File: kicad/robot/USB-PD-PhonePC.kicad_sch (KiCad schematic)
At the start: 44 parts, among them IC1 TPS61253AYFFR, U11 MAX77958EWV+T, U15 ESD122DMYR

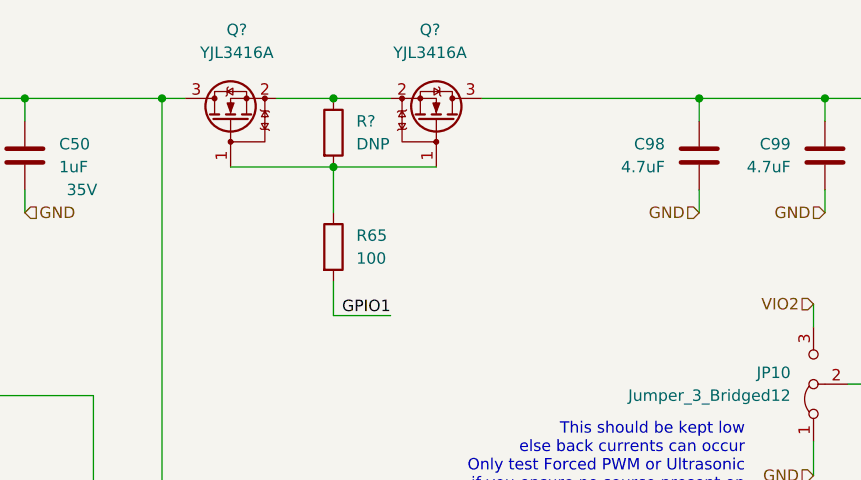
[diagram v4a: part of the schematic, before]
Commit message: Updating mosfets to load switch on phone side USB
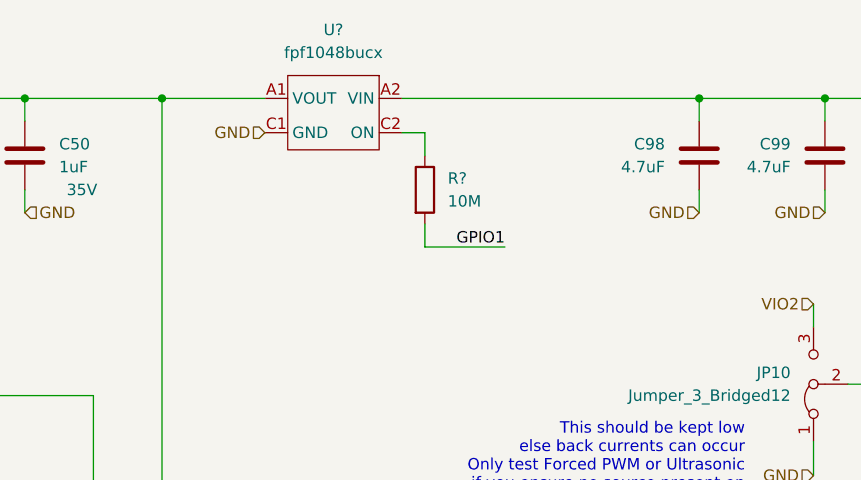
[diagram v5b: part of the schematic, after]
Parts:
- removed Q? (x2): YJL3416A, Package_TO_SOT_SMD:SOT-23, symbol Transistor_FET:YJL3416A
- removed R65: 100, Resistor_SMD:R_0603_1608Metric, symbol Device:R
- removed R?: DNP, Resistor_SMD:R_0603_1608Metric, symbol Device:R
- added R?: 10M, Resistor_SMD:R_0603_1608Metric, symbol Device:R
- added U?: fpf1048bucx, Package_BGA:BGA6N50P3X2_146X96X62N, symbol Power_Management:fpf1048bucx
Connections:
- net GND: now also U?.C1 (GND)
- net GPIO1: now also R?.2
- net at C100.1, C98.1, C99.1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: now also U?.A2 (VIN), U?.B2 (VIN)
- net at C50.1, JP4.2 (B), U11.A6 (VBUS): now also U?.A1 (VOUT), U?.B1 (VOUT)
- new net: R?.1, U?.C2 (ON)
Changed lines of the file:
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@@
   (junction (at 287.02 293.37) (diameter 0) (color 0 0 0 0)
   )
-  (junction (at 267.97 128.27) (diameter 0) (color 0 0 0 0)
-  )
   (junction (at 322.58 120.65) (diameter 0) (color 0 0 0 0)
   )
@@
   )
   (junction (at 236.22 267.97) (diameter 0) (color 0 0 0 0)
-  )
-  (junction (at 267.97 120.65) (diameter 0) (color 0 0 0 0)
   )
   (junction (at 187.96 201.93) (diameter 0) (color 0 0 0 0)
@@
     (stroke (width 0) (type default) (color 0 0 0 0))
   )
-  (wire (pts (xy 267.97 140.97) (xy 267.97 144.78))
-    (stroke (width 0) (type default) (color 0 0 0 0))
-  )
   (wire (pts (xy 397.51 120.65) (xy 410.21 120.65))
     (stroke (width 0) (type default) (color 0 0 0 0))
@@
     (stroke (width 0) (type default) (color 0 0 0 0))
   )
+  (wire (pts (xy 275.59 124.46) (xy 278.13 124.46))
+    (stroke (width 0) (type default) (color 0 0 0 0))
+  )
   (wire (pts (xy 213.36 175.26) (xy 213.36 180.34))
     (stroke (width 0) (type default) (color 0 0 0 0))
@@
     (stroke (width 0) (type default) (color 0 0 0 0))
   )
+  (wire (pts (xy 278.13 134.62) (xy 278.13 137.16))
+    (stroke (width 0) (type default) (color 0 0 0 0))
+  )
   (wire (pts (xy 353.06 280.67) (xy 353.06 283.21))
     (stroke (width 0) (type default) (color 0 0 0 0))
@@
     (stroke (width 0) (type default) (color 0 0 0 0))
   )
+  (wire (pts (xy 248.92 120.65) (xy 260.35 120.65))
+    (stroke (width 0) (type default) (color 0 0 0 0))
+  )
   (wire (pts (xy 331.47 152.4) (xy 331.47 140.97))
     (stroke (width 0) (type default) (color 0 0 0 0))
@@
     (stroke (width 0) (type default) (color 0 0 0 0))
   )
-  (wire (pts (xy 267.97 144.78) (xy 274.32 144.78))
+  (wire (pts (xy 278.13 137.16) (xy 287.02 137.16))
     (stroke (width 0) (type default) (color 0 0 0 0))
   )
@@
     (stroke (width 0) (type default) (color 0 0 0 0))
   )
-  (wire (pts (xy 261.62 120.65) (xy 267.97 120.65))
-    (stroke (width 0) (type default) (color 0 0 0 0))
-  )
   (wire (pts (xy 309.88 254) (xy 316.23 254))
     (stroke (width 0) (type default) (color 0 0 0 0))
@@
     (stroke (width 0) (type default) (color 0 0 0 0))
   )
+  (wire (pts (xy 278.13 124.46) (xy 278.13 127))
+    (stroke (width 0) (type default) (color 0 0 0 0))
+  )
   (wire (pts (xy 219.71 262.89) (xy 219.71 267.97))
     (stroke (width 0) (type default) (color 0 0 0 0))
@@
     (stroke (width 0) (type default) (color 0 0 0 0))
   )
-  (wire (pts (xy 267.97 128.27) (xy 267.97 133.35))
-    (stroke (width 0) (type default) (color 0 0 0 0))
-  )
   (wire (pts (xy 309.88 259.08) (xy 316.23 259.08))
     (stroke (width 0) (type default) (color 0 0 0 0))
@@
     (stroke (width 0) (type default) (color 0 0 0 0))
   )
-  (wire (pts (xy 256.54 128.27) (xy 267.97 128.27))
-    (stroke (width 0) (type default) (color 0 0 0 0))
-  )
   (wire (pts (xy 379.73 120.65) (xy 375.92 120.65))
     (stroke (width 0) (type default) (color 0 0 0 0))
@@
     (stroke (width 0) (type default) (color 0 0 0 0))
   )
-  (wire (pts (xy 267.97 128.27) (xy 279.4 128.27))
-    (stroke (width 0) (type default) (color 0 0 0 0))
-  )
   (wire (pts (xy 200.66 120.65) (xy 213.36 120.65))
     (stroke (width 0) (type default) (color 0 0 0 0))
@@
     (stroke (width 0) (type default) (color 0 0 0 0))
   )
-  (wire (pts (xy 248.92 120.65) (xy 251.46 120.65))
-    (stroke (width 0) (type default) (color 0 0 0 0))
-  )
   (wire (pts (xy 336.55 120.65) (xy 342.9 120.65))
     (stroke (width 0) (type default) (color 0 0 0 0))
@@
     (stroke (width 0) (type default) (color 0 0 0 0))
   )
-  (wire (pts (xy 267.97 120.65) (xy 274.32 120.65))
-    (stroke (width 0) (type default) (color 0 0 0 0))
-  )
   (wire (pts (xy 175.26 228.6) (xy 193.04 228.6))
     (stroke (width 0) (type default) (color 0 0 0 0))
@@
     (stroke (width 0) (type default) (color 0 0 0 0))
   )
-  (wire (pts (xy 284.48 120.65) (xy 308.61 120.65))
+  (wire (pts (xy 275.59 120.65) (xy 308.61 120.65))
     (stroke (width 0) (type default) (color 0 0 0 0))
   )
@@
     (effects (font (size 1.27 1.27)) (justify right bottom))
   )
-  (label "GPIO1" (at 274.32 144.78 180)
+  (label "GPIO1" (at 287.02 137.16 180)
     (effects (font (size 1.27 1.27)) (justify right bottom))
   )
@@
   )
   (hierarchical_label "GND" (shape input) (at 321.31 162.56 180)
+    (effects (font (size 1.27 1.27)) (justify right))
+  )
+  (hierarchical_label "GND" (shape input) (at 260.35 124.46 180)
     (effects (font (size 1.27 1.27)) (justify right))
   )
@@
     (pin "2")
   )
-  (symbol (lib_id "Transistor_FET:YJL3416A") (at 279.4 123.19 270) (mirror x) (unit 1)
-    (in_bom yes) (on_board yes) (fields_autoplaced)
-    (property "Reference" "Q?" (id 0) (at 278.7015 113.03 90))
-    (property "Value" "YJL3416A" (id 1) (at 278.7015 115.57 90))
-    (property "Footprint" "Package_TO_SOT_SMD:SOT-23" (id 2) (at 277.495 118.11 0)
-      (effects (font (size 1.27 1.27)) (justify left) hide)
-    )
-    (property "Datasheet" "https://www.21yangjie.com/style/pdf/low-voltage-mosfet/YJL3416A.pdf" (id 3) (at 279.4 123.19 0)
-      (effects (font (size 1.27 1.27)) hide)
-    )
-    (pin "1")
-    (pin "2")
-    (pin "3")
-  )
   (symbol (lib_id "Jumper:Jumper_2_Bridged") (at 177.8 201.93 0) (unit 1)
     (in_bom yes) (on_board yes) (fields_autoplaced)
@@
     (pin "1")
   )
-  (symbol (lib_id "Transistor_FET:YJL3416A") (at 256.54 123.19 90) (unit 1)
-    (in_bom yes) (on_board yes) (fields_autoplaced)
-    (property "Reference" "Q?" (id 0) (at 257.2385 113.03 90))
-    (property "Value" "YJL3416A" (id 1) (at 257.2385 115.57 90))
-    (property "Footprint" "Package_TO_SOT_SMD:SOT-23" (id 2) (at 258.445 118.11 0)
-      (effects (font (size 1.27 1.27)) (justify left) hide)
-    )
-    (property "Datasheet" "https://www.21yangjie.com/style/pdf/low-voltage-mosfet/YJL3416A.pdf" (id 3) (at 256.54 123.19 0)
-      (effects (font (size 1.27 1.27)) hide)
-    )
-    (pin "1")
-    (pin "2")
-    (pin "3")
-  )
   (symbol (lib_id "Device:R") (at 353.06 287.02 0) (unit 1)
     (in_bom yes) (on_board yes) (fields_autoplaced)
@@
     (pin "2")
   )
-  (symbol (lib_id "Device:R") (at 267.97 124.46 0) (unit 1)
-    (in_bom yes) (on_board yes) (fields_autoplaced)
-    (property "Reference" "R?" (id 0) (at 270.51 123.1899 0)
-      (effects (font (size 1.27 1.27)) (justify left))
-    )
-    (property "Value" "DNP" (id 1) (at 270.51 125.7299 0)
-      (effects (font (size 1.27 1.27)) (justify left))
-    )
-    (property "Footprint" "Resistor_SMD:R_0603_1608Metric" (id 2) (at 266.192 124.46 90)
-      (effects (font (size 1.27 1.27)) hide)
-    )
-    (property "Datasheet" "~" (id 3) (at 267.97 124.46 0)
-      (effects (font (size 1.27 1.27)) hide)
-    )
-    (pin "1")
-    (pin "2")
-  )
   (symbol (lib_id "Device:C") (at 231.14 259.08 0) (unit 1)
     (in_bom yes) (on_board yes)
@@
     (pin "2")
     (pin "3")
+  )
+  (symbol (lib_id "Power_Management:fpf1048bucx") (at 267.97 121.92 0) (mirror y) (unit 1)
+    (in_bom yes) (on_board yes) (fields_autoplaced)
+    (property "Reference" "U?" (id 0) (at 267.97 113.03 0))
+    (property "Value" "fpf1048bucx" (id 1) (at 267.97 115.57 0))
+    (property "Footprint" "Package_BGA:BGA6N50P3X2_146X96X62N" (id 2) (at 268.605 122.555 0)
+      (effects (font (size 1.27 1.27)) hide)
+    )
+    (property "Datasheet" "https://octopart.com/datasheet/fpf1048bucx-onsemi-84327717" (id 3) (at 268.605 122.555 0)
+      (effects (font (size 1.27 1.27)) hide)
+    )
+    (property "Part Number" "fpf1048bucx" (id 4) (at 267.97 121.92 0)
+      (effects (font (size 1.27 1.27)) hide)
+    )
+    (pin "A1")
+    (pin "A2")
+    (pin "B1")
+    (pin "B2")
+    (pin "C1")
+    (pin "C2")
   )
   (symbol (lib_id "Device:R") (at 339.09 273.05 0) (unit 1)
@@
     (pin "1")
   )
+  (symbol (lib_id "Device:R") (at 278.13 130.81 0) (unit 1)
+    (in_bom yes) (on_board yes) (fields_autoplaced)
+    (property "Reference" "R?" (id 0) (at 280.67 129.5399 0)
+      (effects (font (size 1.27 1.27)) (justify left))
+    )
+    (property "Value" "10M" (id 1) (at 280.67 132.0799 0)
+      (effects (font (size 1.27 1.27)) (justify left))
+    )
+    (property "Footprint" "Resistor_SMD:R_0603_1608Metric" (id 2) (at 276.352 130.81 90)
+      (effects (font (size 1.27 1.27)) hide)
+    )
+    (property "Datasheet" "~" (id 3) (at 278.13 130.81 0)
+      (effects (font (size 1.27 1.27)) hide)
+    )
+    (pin "1")
+    (pin "2")
+  )
   (symbol (lib_id "Device:C") (at 336.55 127 0) (mirror y) (unit 1)
     (in_bom yes) (on_board yes)
@@
       (effects (font (size 1.27 1.27)) hide)
     )
-    (pin "1")
-    (pin "2")
-  )
-  (symbol (lib_id "Device:R") (at 267.97 137.16 0) (unit 1)
-    (in_bom yes) (on_board yes) (fields_autoplaced)
-    (property "Reference" "R65" (id 0) (at 270.51 135.8899 0)
-      (effects (font (size 1.27 1.27)) (justify left))
-    )
-    (property "Value" "100" (id 1) (at 270.51 138.4299 0)
-      (effects (font (size 1.27 1.27)) (justify left))
-    )
-    (property "Footprint" "Resistor_SMD:R_0603_1608Metric" (id 2) (at 266.192 137.16 90)
-      (effects (font (size 1.27 1.27)) hide)
-    )
-    (property "Datasheet" "~" (id 3) (at 267.97 137.16 0)
-      (effects (font (size 1.27 1.27)) hide)
-    )

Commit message: Annotated recent changes
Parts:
- gave numbers to parts that had none: 2
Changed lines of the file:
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@@
   (symbol (lib_id "Power_Management:fpf1048bucx") (at 267.97 121.92 0) (mirror y) (unit 1)
     (in_bom yes) (on_board yes) (fields_autoplaced)
-    (property "Reference" "U?" (id 0) (at 267.97 113.03 0))
+    (property "Reference" "U16" (id 0) (at 267.97 113.03 0))
     (property "Value" "fpf1048bucx" (id 1) (at 267.97 115.57 0))
     (property "Footprint" "Package_BGA:BGA6N50P3X2_146X96X62N" (id 2) (at 268.605 122.555 0)
@@
   (symbol (lib_id "Device:R") (at 278.13 130.81 0) (unit 1)
     (in_bom yes) (on_board yes) (fields_autoplaced)
-    (property "Reference" "R?" (id 0) (at 280.67 129.5399 0)
-      (effects (font (size 1.27 1.27)) (justify left))
-    )
+    (property "Reference" "R65" (id 0) (at 280.67 129.5399 0)
+      (effects (font (size 1.27 1.27)) (justify left))
+    )

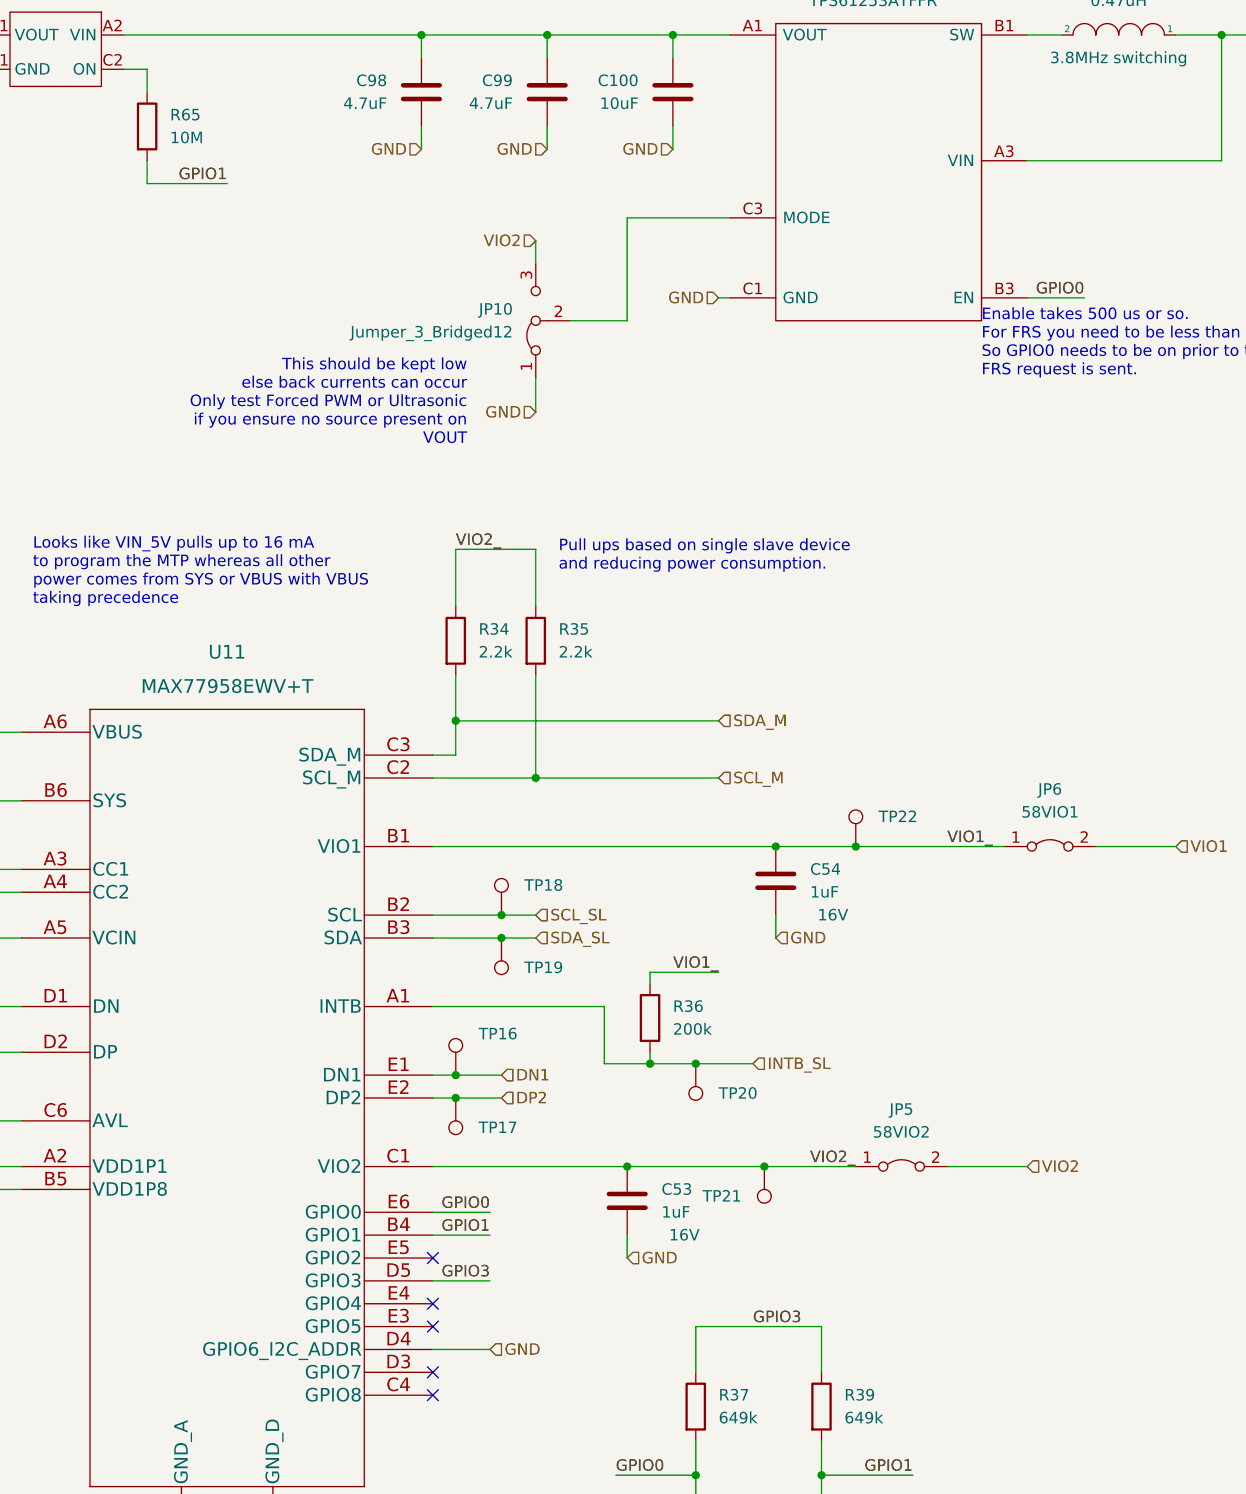
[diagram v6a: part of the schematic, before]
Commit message: Updated conflicint GPIO pins on USB-PD-PhonePC
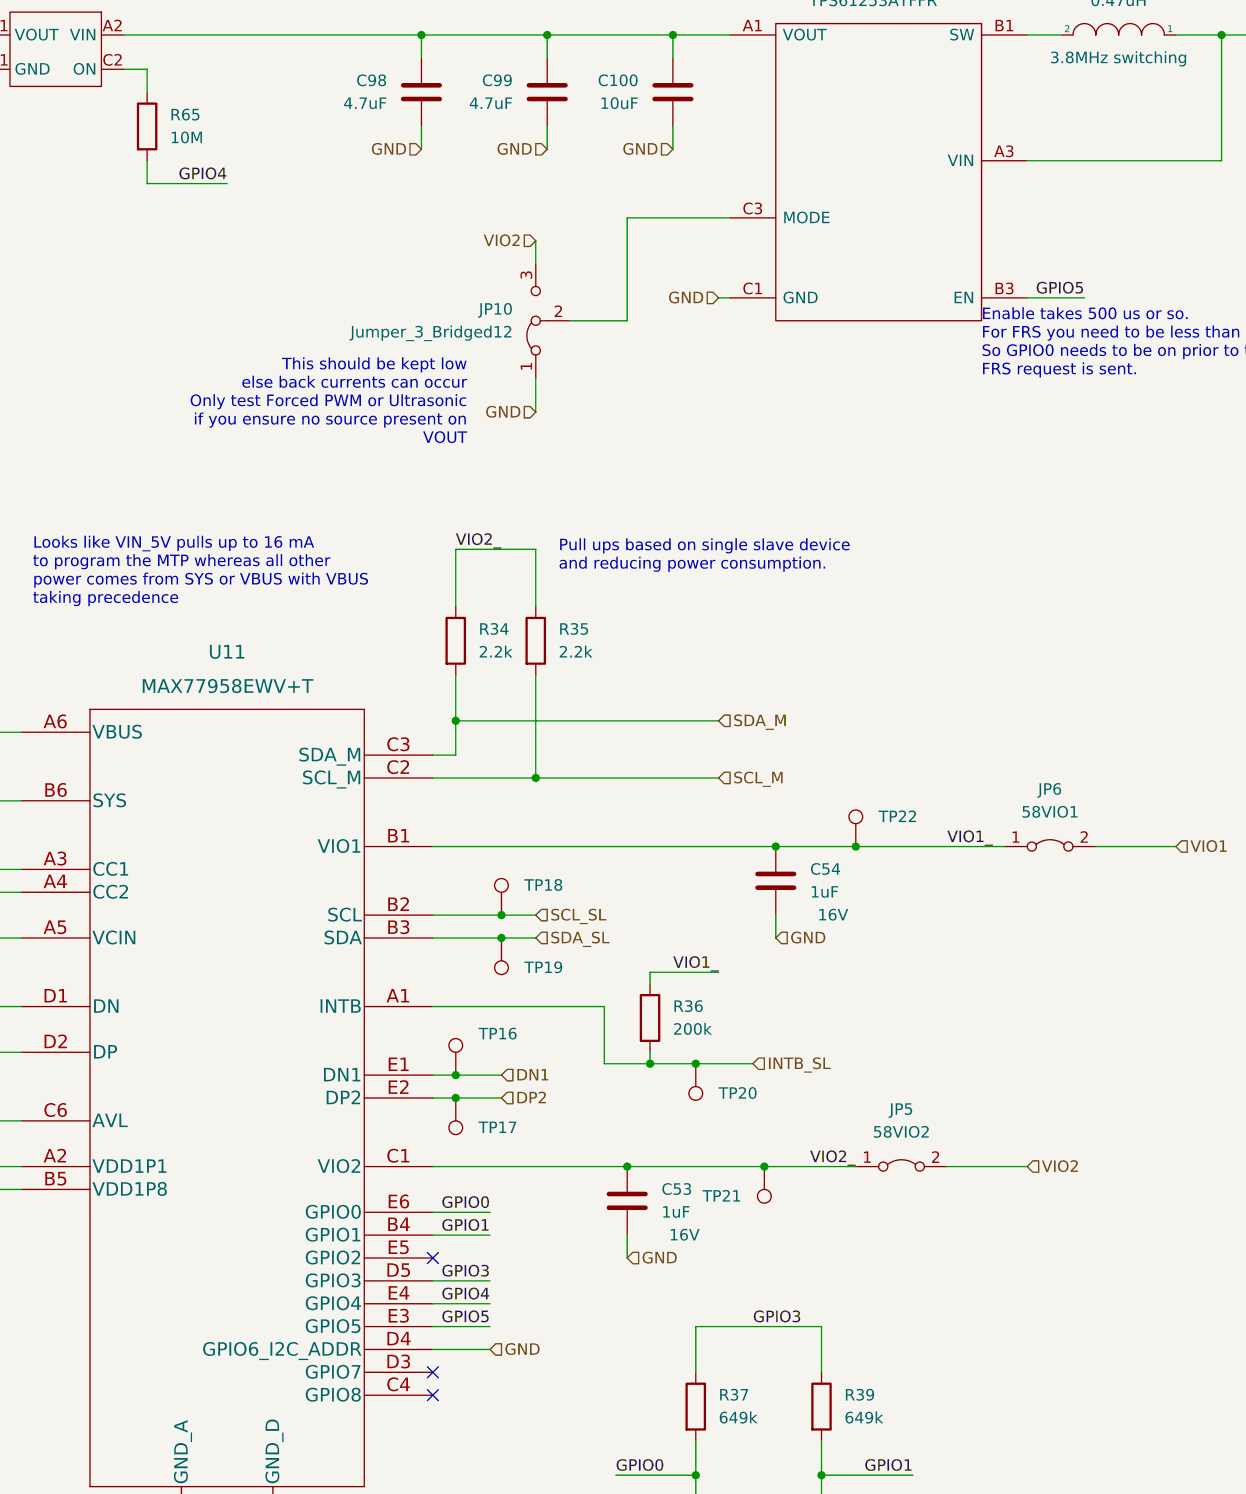
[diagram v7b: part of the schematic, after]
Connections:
- net GPIO0: no longer IC1.B3 (EN)
- net GPIO1: no longer R65.2
- net GPIO5: now reaches U11.E3 (GPIO5)
- net GPIO5: now also IC1.B3 (EN)
- net GPIO4: now reaches U11.E4 (GPIO4)
- net GPIO4: now also R65.2
- no-connect marks 5 -> 3
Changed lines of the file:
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@@
   )
   (no_connect (at 309.88 256.54))
-  (no_connect (at 309.88 261.62))
-  (no_connect (at 309.88 264.16))
   (no_connect (at 309.88 269.24))
   (no_connect (at 309.88 271.78))
@@
     (stroke (width 0) (type default) (color 0 0 0 0))
   )
+  (wire (pts (xy 309.88 264.16) (xy 316.23 264.16))
+    (stroke (width 0) (type default) (color 0 0 0 0))
+  )
   (wire (pts (xy 223.52 120.65) (xy 233.68 120.65))
     (stroke (width 0) (type default) (color 0 0 0 0))
@@
   )
   (wire (pts (xy 321.31 184.15) (xy 321.31 177.8))
+    (stroke (width 0) (type default) (color 0 0 0 0))
+  )
+  (wire (pts (xy 309.88 261.62) (xy 316.23 261.62))
     (stroke (width 0) (type default) (color 0 0 0 0))
   )
@@
     (effects (font (size 1.27 1.27)) (justify right bottom))
   )
-  (label "GPIO1" (at 287.02 137.16 180)
+  (label "GPIO4" (at 287.02 137.16 180)
     (effects (font (size 1.27 1.27)) (justify right bottom))
   )
@@
     (effects (font (size 1.27 1.27)) (justify right bottom))
   )
-  (label "GPIO0" (at 382.27 149.86 180)
+  (label "GPIO5" (at 382.27 149.86 180)
     (effects (font (size 1.27 1.27)) (justify right bottom))
   )
@@
     (effects (font (size 1.27 1.27)) (justify left bottom))
   )
+  (label "GPIO4" (at 316.23 261.62 180)
+    (effects (font (size 1.27 1.27)) (justify right bottom))
+  )
   (label "VIO2_" (at 351.79 246.38 0)
     (effects (font (size 1.27 1.27)) (justify left bottom))
   )
+  (label "GPIO5" (at 316.23 264.16 180)
+    (effects (font (size 1.27 1.27)) (justify right bottom))
+  )
   (label "GPIO1" (at 363.22 280.67 180)
